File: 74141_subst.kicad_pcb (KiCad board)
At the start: 2 copper layers, 19.9 x 9.4 mm, 14 parts, among them Q1 NHUMD12, Q2 NHUMD12, Q3 NHUMD12, Q4 NHUMD12, Q5 NHUMD12, U1 CD4028BPWR, U2 74141-SOCKET, U3 74HCT08

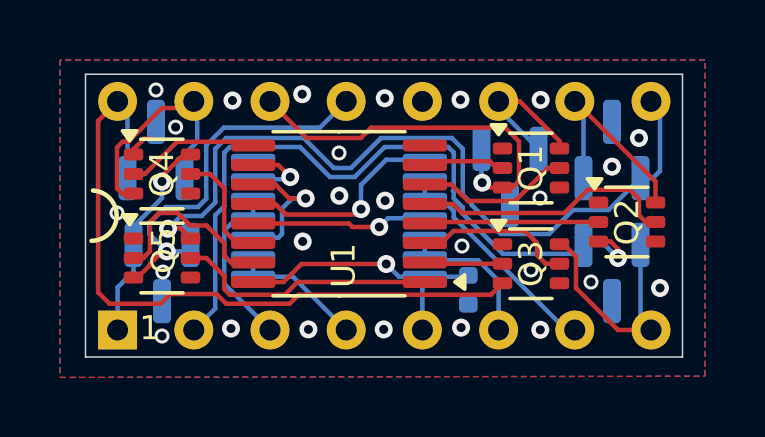
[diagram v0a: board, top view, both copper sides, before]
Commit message: Added info in silk
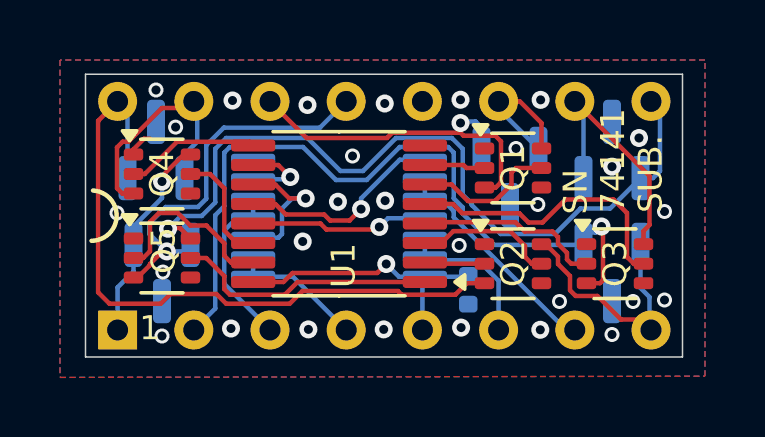
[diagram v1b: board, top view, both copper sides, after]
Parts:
- moved Q3 1.45 mm to (145.0, 91.8)
- moved Q2 0.60 mm to (141.6, 91.8)
- moved Q1 0.60 mm to (141.6, 88.6)
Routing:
- net /Q7: track 7.17 -> 8.55 mm
- net /Q5: track 13.2 -> 12.2 mm
- net /Q9: track 24.2 -> 25.2 mm
- net /S9: track 8.90 -> 9.60 mm
- net /S0: track 5.34 -> 4.71 mm
- net /S2: track 2.60 -> 2.00 mm
- net /S6: track 2.53 -> 2.03 mm
- net GND: vias 26 -> 29
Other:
- board text added: "74141"
- board text added: "SN"
- board text added: "SUB."
